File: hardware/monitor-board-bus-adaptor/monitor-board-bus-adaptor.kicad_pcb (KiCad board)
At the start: 2 copper layers, 80 x 100 mm, 9 parts, among them P1 CTRL1, P2 CTRL2, P3 IO, P4 ADDR1, P5 ADDR2, P6 DATA, P7 CTRL_BUS, P8 AD_BUS

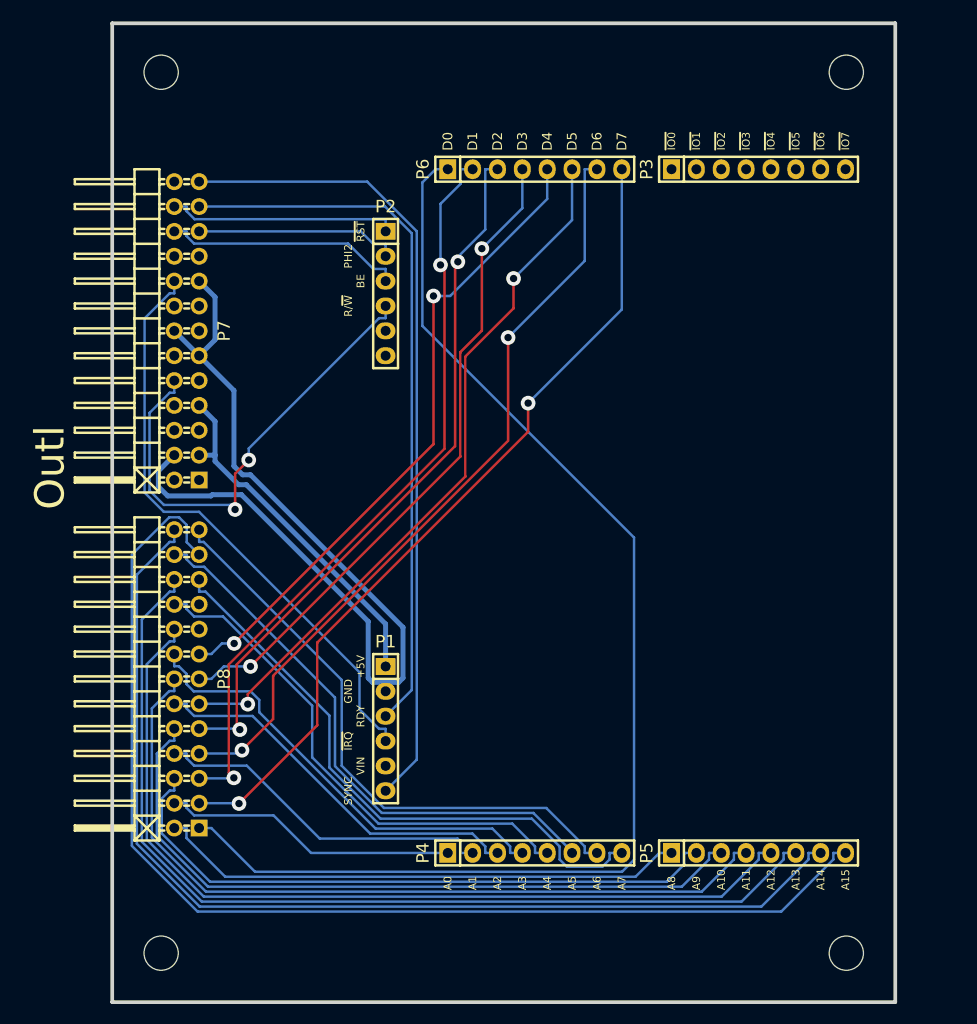
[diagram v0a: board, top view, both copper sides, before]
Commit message: correct socket layout on bus adaptor
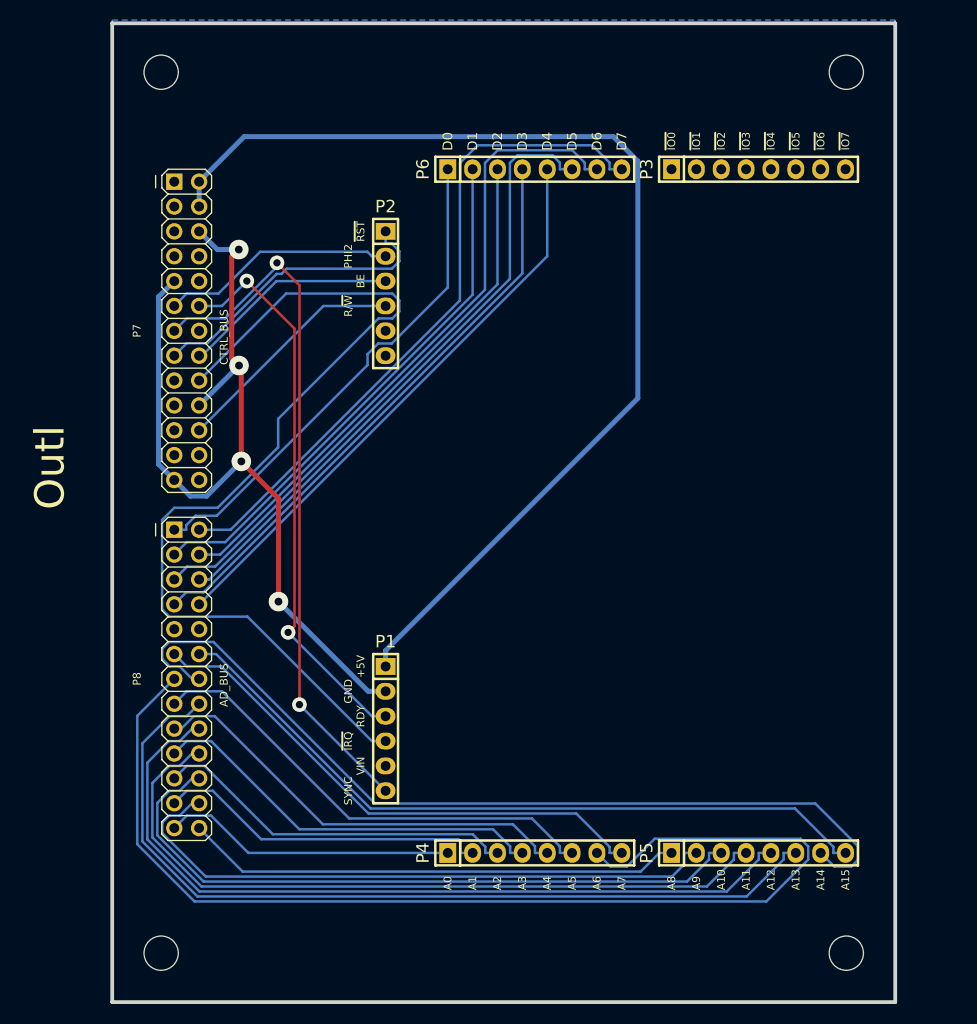
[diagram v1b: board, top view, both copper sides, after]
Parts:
- P7, P8: footprint Pin_Headers:Pin_Header_Angled_2x13 -> ab2tech:AB2_HDR_M13-2V
- turned P7 to 270 degrees
- turned P8 to 270 degrees
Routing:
- net /D0: track 128.1 -> 51.2 mm
- net +5V: track 36.7 -> 112.6 mm
- net /A6: track 60.6 -> 116.2 mm
- net /A15: track 119.4 -> 74.8 mm
- net ~IRQ: track 61.2 -> 97.8 mm
- net R/~W: track 49.7 -> 24.3 mm, vias 2 -> 0
- net /D1: track 77.4 -> 54.3 mm, vias 2 -> 0
- net /A14: track 109.1 -> 91.7 mm
- net /D2: track 73.3 -> 57.3 mm, vias 2 -> 0
- net /D7: track 85.1 -> 69.1 mm, vias 2 -> 0
- net RDY: track 73.3 -> 57.6 mm, vias 0 -> 2
- net /D6: track 79.6 -> 66.5 mm, vias 2 -> 0
- net /A13: track 100.2 -> 88.8 mm
- net SYNC: track 82.8 -> 72.1 mm, vias 0 -> 2
- net /D5: track 73.4 -> 64.0 mm, vias 2 -> 0
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- added copper zone on B.Cu, net GND

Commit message: re-factor bus adaptor
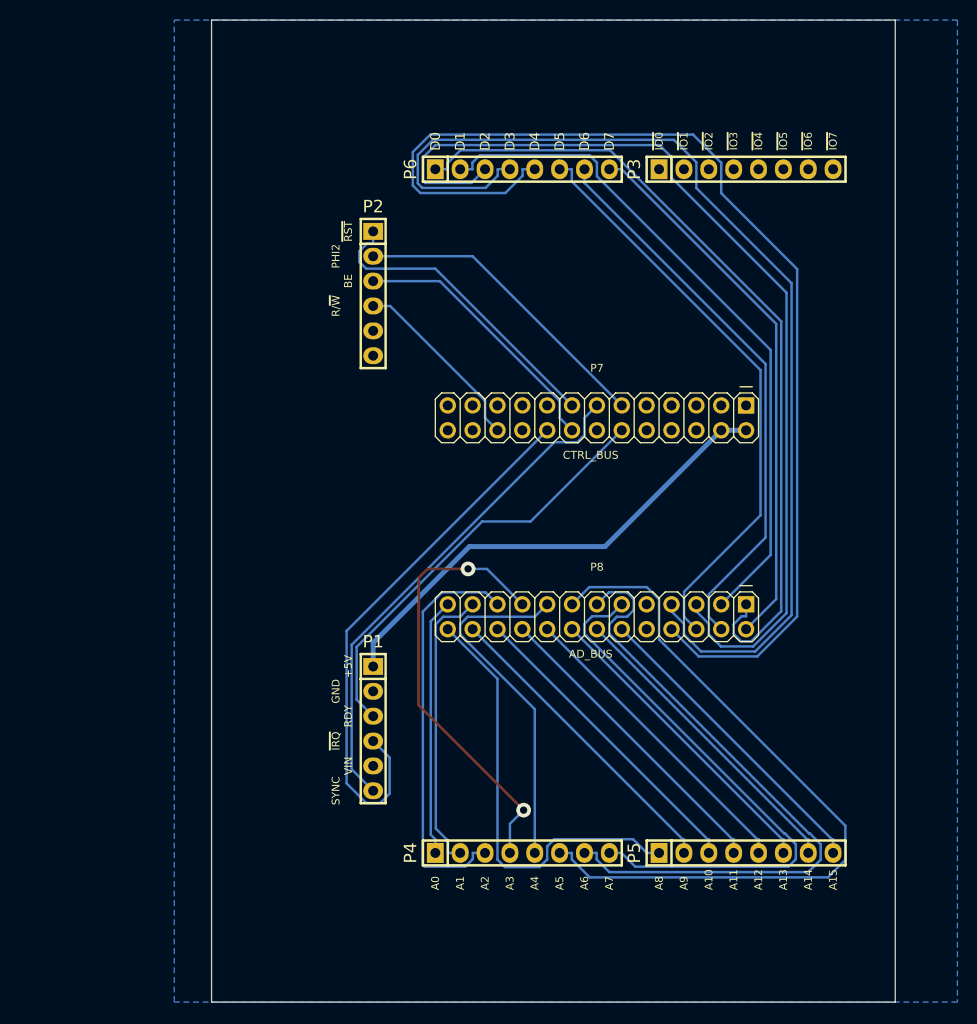
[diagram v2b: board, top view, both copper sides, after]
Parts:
- removed Outl: EuroBoard_halb_Type-I_100mmX80mm_holes, EuroBoard_Outline:EuroBoard_halb_Type-I_100mmX80mm_holes
- moved P7 42.8 mm to (114.3, 97.8), turned to 180 degrees
- moved P8 42.4 mm to (114.3, 118.1), turned to 180 degrees
- moved P3 1.27 mm to (129.5, 72.4)
- moved P5 1.27 mm to (129.5, 142.2)
- moved P1 1.27 mm to (91.4, 129.5)
- moved P2 1.27 mm to (91.4, 85.1)
- moved P4 1.27 mm to (106.7, 142.2)
- moved P6 1.27 mm to (106.7, 72.4)
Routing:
- net GND: track 94.2 -> 0.00 mm, vias 4 -> 0
- net +5V: track 112.6 -> 49.5 mm
- net /A14: track 91.7 -> 31.9 mm
- net /D4: track 59.2 -> 116.3 mm
- net /A13: track 88.8 -> 31.9 mm
- net /D3: track 60.2 -> 110.9 mm
- net /A12: track 82.5 -> 31.9 mm
- net /A6: track 116.2 -> 67.7 mm
- net /A11: track 76.1 -> 31.9 mm
- net /D2: track 57.3 -> 100.7 mm
- net /A15: track 74.8 -> 31.9 mm
- net ~IRQ: track 97.8 -> 56.3 mm
- net /A10: track 69.8 -> 31.9 mm
- net /D0: track 51.2 -> 83.6 mm
- net /A9: track 63.8 -> 31.9 mm
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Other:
- board size 80 x 100 mm -> 69.8 x 100.3 mm

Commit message: bus adaptor: make layout more home-PCB friendly
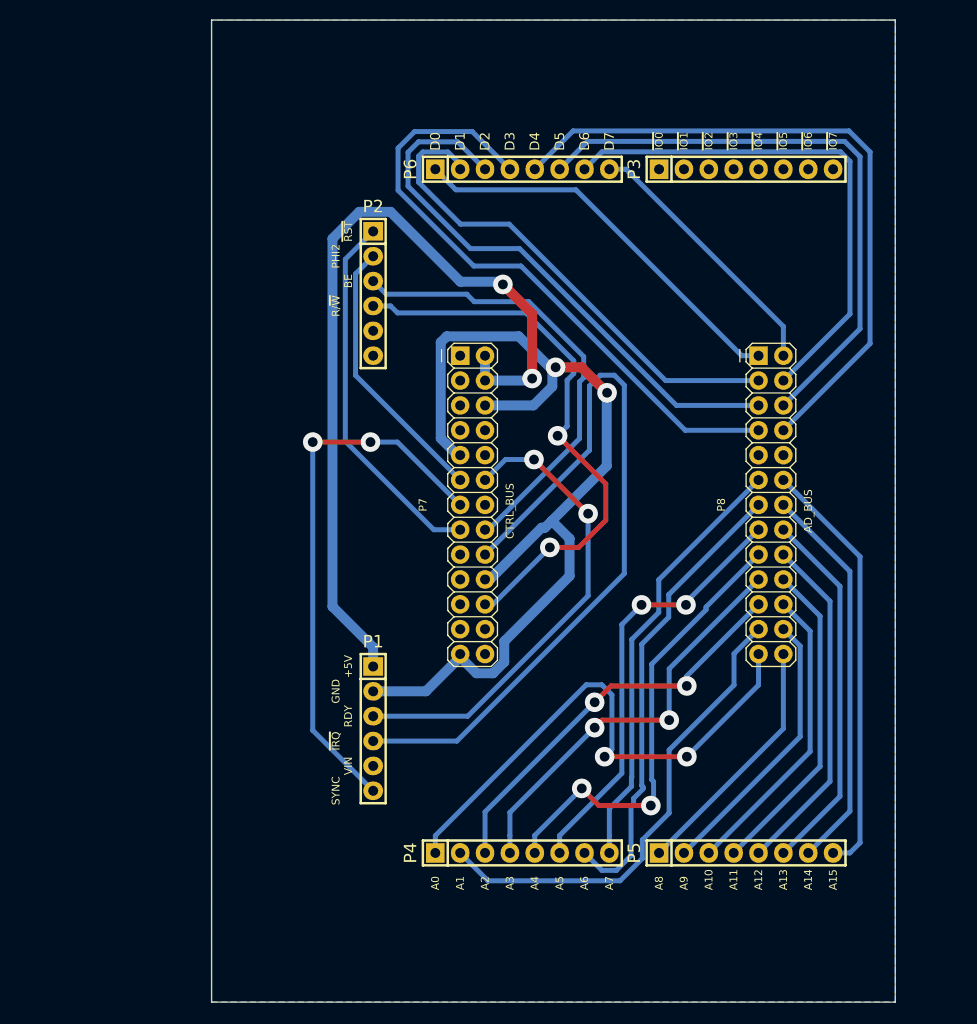
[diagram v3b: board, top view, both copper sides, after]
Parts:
- moved P8 21.1 mm to (132.1, 106.7), turned to 270 degrees
- moved P7 15.5 mm to (101.6, 106.7), turned to 270 degrees
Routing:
- net GND: track 0.00 -> 100.7 mm, vias 0 -> 2
- net /D4: track 116.3 -> 68.9 mm
- net /D3: track 110.9 -> 65.0 mm
- net /D0: track 83.6 -> 40.9 mm
- net /D2: track 100.7 -> 58.0 mm
- net R/~W: track 19.0 -> 57.7 mm, vias 0 -> 2
- net +5V: track 49.5 -> 85.3 mm, vias 0 -> 2
- net /A5: track 76.0 -> 44.1 mm, vias 0 -> 2
- net /A0: track 26.3 -> 55.2 mm, vias 0 -> 2
- net /D7: track 56.1 -> 27.4 mm
- net ~IRQ: track 56.3 -> 78.1 mm
- net /A6: track 67.7 -> 47.5 mm
- net /A8: track 45.0 -> 25.6 mm
- net /A1: track 29.7 -> 49.1 mm
- net BE: track 27.6 -> 46.8 mm
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- added copper zone on B.Cu, net (none)
- removed copper zone on B.Cu, net GND
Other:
- net class Default: clearance 0.254 -> 0.508; trace_width 0.254 -> 0.508; via_dia 1.5 -> 2; via_drill 0.8 -> 1
- net class Power: trace_width 0.508 -> 1.016; via_drill 0.8 -> 1
- rule trace_clearance: 0.254 -> 0.508
